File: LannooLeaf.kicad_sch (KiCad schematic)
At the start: 15 parts, among them J1 Conn_01x01, J12 Conn_02x04_Counter_Clockwise, J2 Conn_01x01, J3 Conn_01x01, J4 Conn_01x01, J5 Conn_02x04_Counter_Clockwise, J6 Conn_02x10_Counter_Clockwise, J7 Conn_02x10_Counter_Clockwise

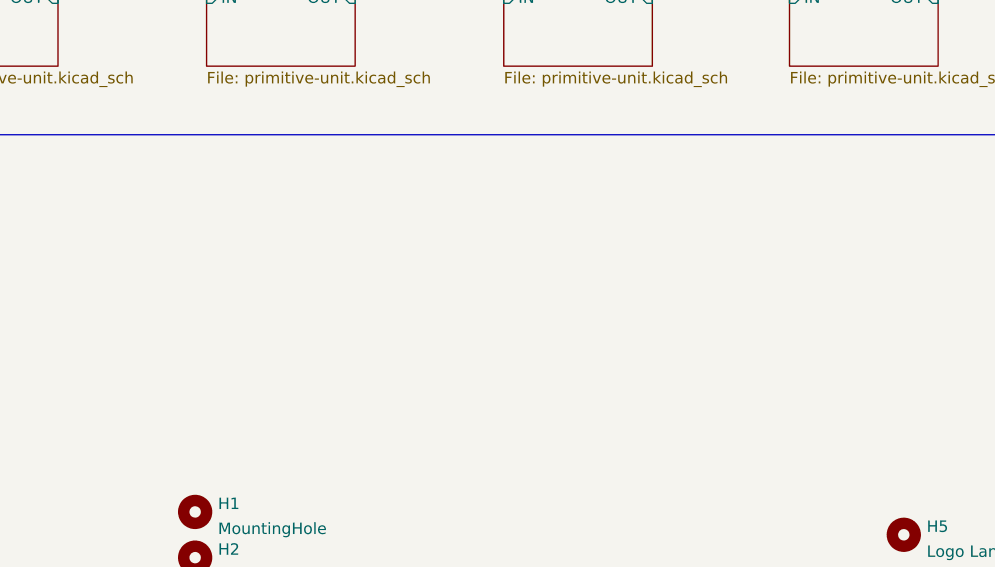
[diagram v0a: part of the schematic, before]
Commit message: add extra 5V caps
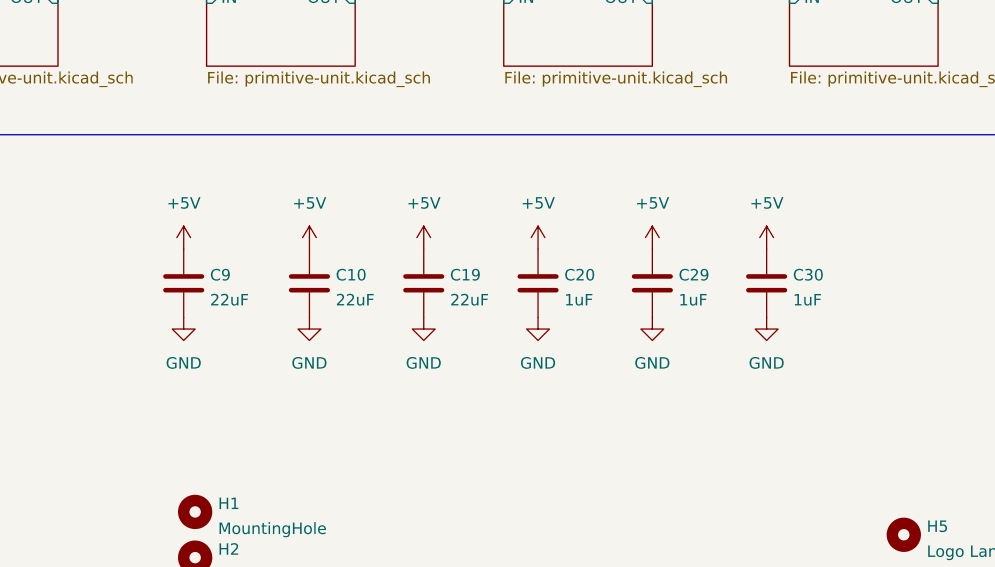
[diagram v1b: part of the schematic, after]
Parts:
- added C10, C19, C9: 22uF, Capacitor_SMD:C_1206_3216Metric, symbol Device:C
- added C20, C29, C30: 1uF, Capacitor_SMD:C_0603_1608Metric, symbol Device:C
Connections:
- net +5V: now also C10.1, C19.1, C20.1, C29.1, C30.1, C9.1
- net GND: now also C10.2, C19.2, C20.2, C29.2, C30.2, C9.2
